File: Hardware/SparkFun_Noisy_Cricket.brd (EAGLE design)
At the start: 31.8 x 25.4 mm, 28 parts, among them U1 LM4853

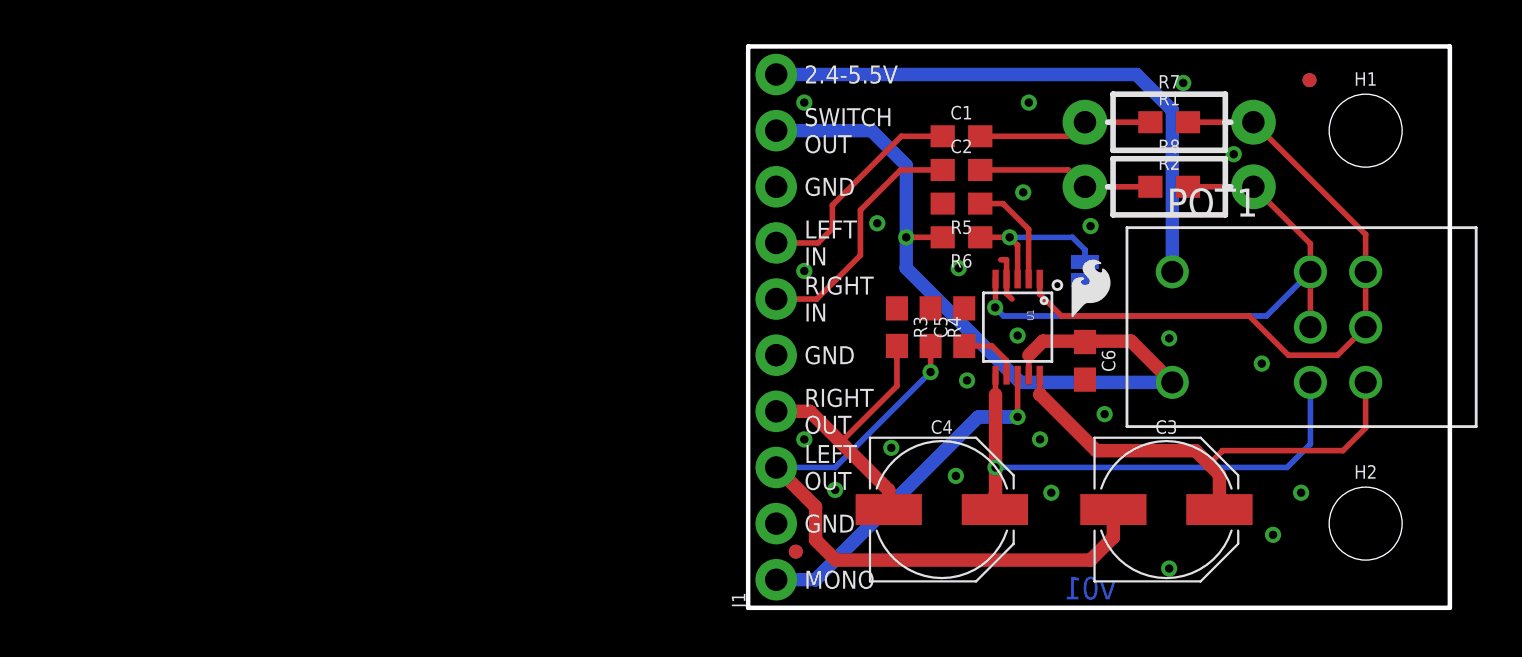
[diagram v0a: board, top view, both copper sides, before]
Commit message: Design Review Changes
- Moved JP1 further away from POT1
- Added JP2 to short C3 and increase bass frequency reponse in mono
operation
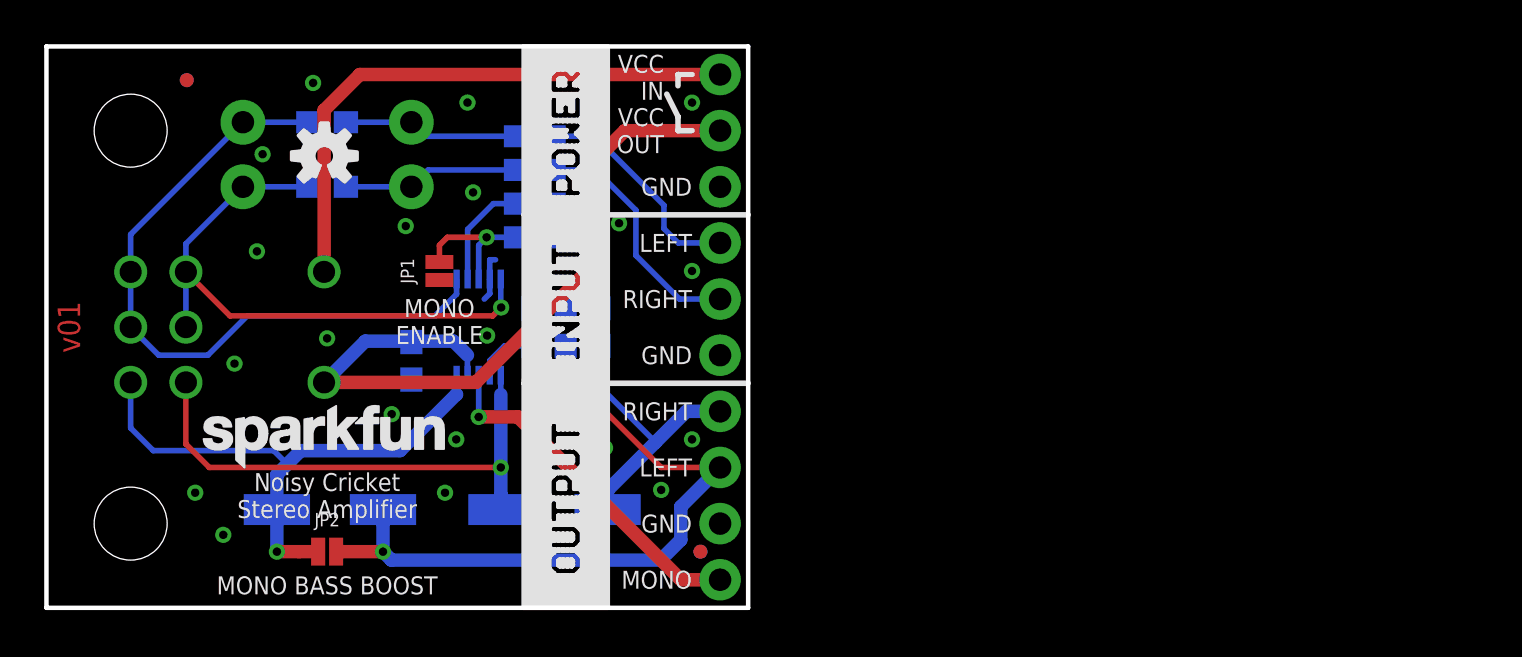
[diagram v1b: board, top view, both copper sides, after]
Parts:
- added JP2: (no value), SparkFun-Jumpers:SMT-JUMPER_2_NO_NO-SILK
- C1, C2: value 0.1uF -> 1.0uF
- moved H1 55.9 mm to (-27.9, 21.6), flipped to the bottom
- moved H2 55.9 mm to (-27.9, 3.81), flipped to the bottom
- moved POT1 55.9 mm to (-27.9, 12.7), flipped to the bottom
- moved FD2 50.8 mm to (-25.4, 23.9), flipped to the bottom
- moved FD4 50.8 mm to (-25.4, 23.9), flipped to the top
- moved LOGO1 50.3 mm to (-25.1, 5.84), flipped to the top
- moved LOGO2 42.5 mm to (-19.2, 20.4), flipped to the top
- moved R1 38.1 mm to (-19.1, 22.0), flipped to the bottom
- moved R2 38.1 mm to (-19.1, 19.1), flipped to the bottom
- moved R7 38.1 mm to (-19.1, 22.0), flipped to the bottom
- moved R8 38.1 mm to (-19.1, 19.1), flipped to the bottom
- moved C3 37.8 mm to (-18.9, 4.45), flipped to the bottom
- moved C6 30.5 mm to (-15.2, 11.2), flipped to the bottom
- moved JP1 29.2 mm to (-14.0, 15.2), flipped to the top
- moved U$1 28.7 mm to (-14.4, 12.8), flipped to the bottom
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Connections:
- removed net N$8: C3.+, POT1.A3, U1.LOUT
- new net LOUT+: C3.+, JP2.1, POT1.A3, U1.LOUT
- net LOUT: now also JP2.2
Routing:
- net LOUT+: track 0.00 -> 25.7 mm, vias 0 -> 1
- net N$8: track 21.9 -> 0.00 mm
- net LOUT: track 29.5 -> 32.0 mm, vias 1 -> 2
- net MODE: track 7.56 -> 6.41 mm
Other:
- board text added: "MONO BASS BOOST"

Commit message: Corrected board position
- Board was saved upside down, corrected by flipping board back around
and resaving.
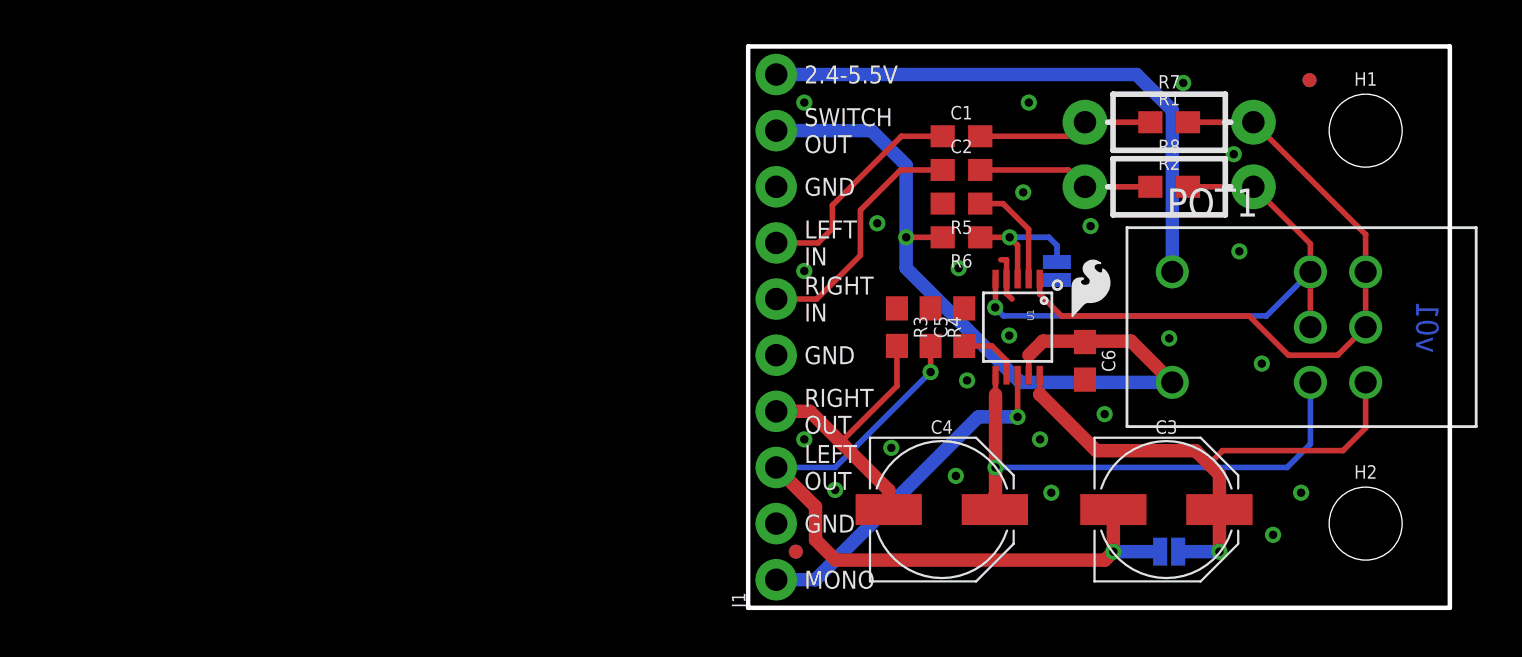
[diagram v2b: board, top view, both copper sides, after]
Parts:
- moved H1 55.9 mm to (27.9, 21.6), flipped to the top
- moved H2 55.9 mm to (27.9, 3.81), flipped to the top
- moved POT1 55.9 mm to (27.9, 12.7), flipped to the top
- moved FD2 50.8 mm to (25.4, 23.9), flipped to the top
- moved FD4 50.8 mm to (25.4, 23.9), flipped to the bottom
- moved LOGO1 50.3 mm to (25.1, 5.84), flipped to the bottom
- moved LOGO2 38.4 mm to (19.2, 20.4), flipped to the bottom
- moved JP2 38.1 mm to (19.1, 2.54), flipped to the bottom
- moved R1 38.1 mm to (19.1, 22.0), flipped to the top
- moved R2 38.1 mm to (19.1, 19.1), flipped to the top
- moved R7 38.1 mm to (19.1, 22.0), flipped to the top
- moved R8 38.1 mm to (19.1, 19.1), flipped to the top
- moved C3 37.8 mm to (18.9, 4.45), flipped to the top
- moved C6 30.5 mm to (15.2, 11.2), flipped to the top
- moved U$1 28.7 mm to (14.4, 12.8), flipped to the top
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
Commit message: v10 Changes
- Replaced C1/C2 with X7R capacitors with a better low end frequency
response.
- Moved C3/C4 further away from POT1.
- Replaced R1/R2 with 2.2k resistors instead of 20k.
- Added lines to top silk to separate Power/Input/Output sections.
- Changed "Mono Enable" silk on bottom layer to "Mono Output".
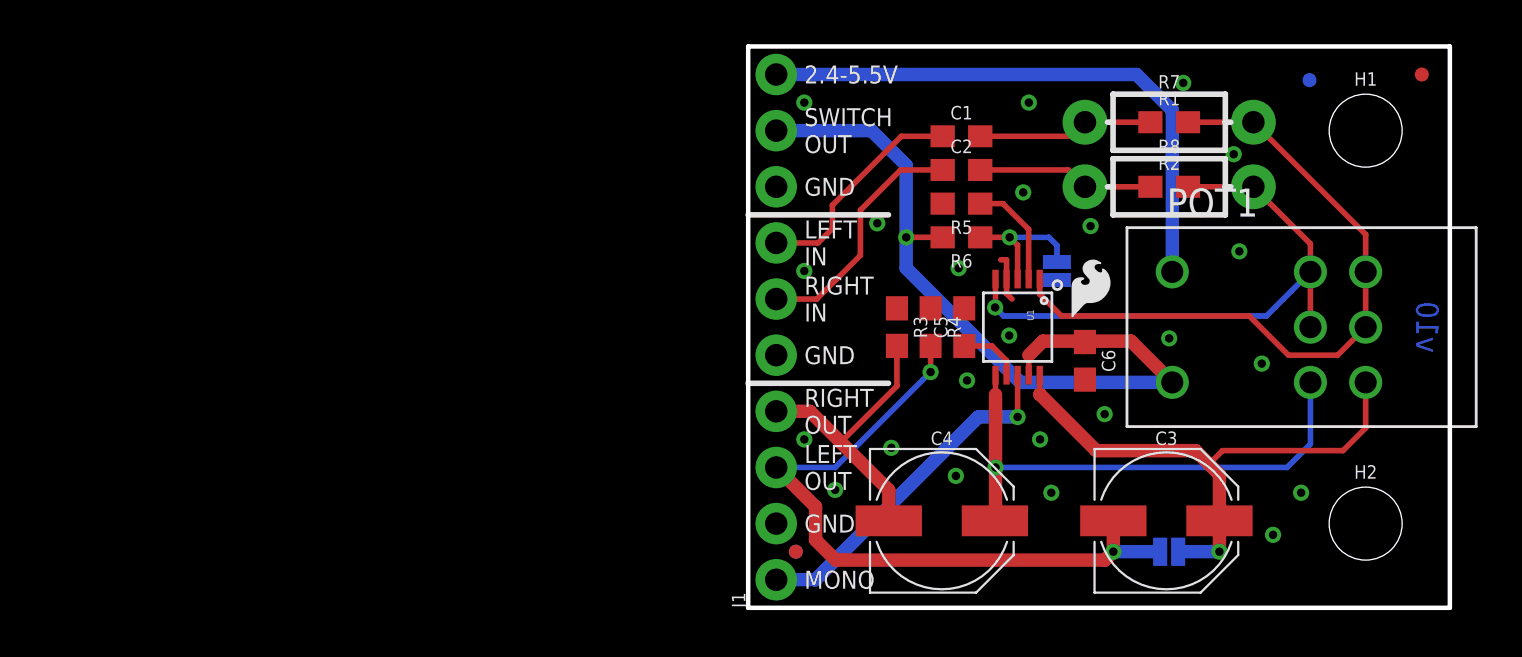
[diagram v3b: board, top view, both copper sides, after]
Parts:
- R1, R2: value 20k -> 2.2k
- moved FD2 5.09 mm to (30.5, 24.1)
- moved POT1 2.54 mm to (25.4, 12.7)
- moved C3 0.51 mm to (18.9, 3.94)
- moved C4 0.51 mm to (8.76, 3.94)
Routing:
- net LOUT: track 32.0 -> 31.5 mm
- net ROUT: track 12.9 -> 13.4 mm
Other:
- board text added: "MONO OUTPUT"
- board text added: "Units: Inches"
- board text added: "v10"
- board text removed: "MONO ENABLE"
- board text removed: "v01"
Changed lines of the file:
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@@
 <layer number="20" name="Dimension" color="15" fill="1" visible="yes" active="yes"/>
 <layer number="21" name="tPlace" color="16" fill="1" visible="yes" active="yes"/>
-<layer number="22" name="bPlace" color="14" fill="1" visible="no" active="yes"/>
+<layer number="22" name="bPlace" color="14" fill="1" visible="yes" active="yes"/>
 <layer number="23" name="tOrigins" color="15" fill="1" visible="yes" active="yes"/>
-<layer number="24" name="bOrigins" color="15" fill="1" visible="no" active="yes"/>
+<layer number="24" name="bOrigins" color="15" fill="1" visible="yes" active="yes"/>
 <layer number="25" name="tNames" color="7" fill="1" visible="no" active="yes"/>
 <layer number="26" name="bNames" color="7" fill="1" visible="no" active="yes"/>
@@
 <layer number="45" name="Holes" color="7" fill="1" visible="no" active="yes"/>
 <layer number="46" name="Milling" color="3" fill="1" visible="no" active="yes"/>
-<layer number="47" name="Measures" color="7" fill="1" visible="no" active="yes"/>
+<layer number="47" name="Measures" color="7" fill="1" visible="yes" active="yes"/>
 <layer number="48" name="Document" color="7" fill="1" visible="no" active="yes"/>
 <layer number="49" name="Reference" color="7" fill="1" visible="no" active="yes"/>
@@
 <layer number="59" name="tCarbon" color="7" fill="1" visible="no" active="no"/>
 <layer number="60" name="bCarbon" color="7" fill="1" visible="no" active="no"/>
+<layer number="88" name="SimResults" color="9" fill="1" visible="yes" active="yes"/>
+<layer number="89" name="SimProbes" color="9" fill="1" visible="yes" active="yes"/>
 <layer number="90" name="Modules" color="5" fill="1" visible="no" active="no"/>
 <layer number="91" name="Nets" color="2" fill="1" visible="no" active="no"/>
@@
 <text x="2.54" y="1.27" size="0.8128" layer="22" font="vector" ratio="15" rot="MR180" align="center-left">MONO</text>
 <text x="13.97" y="12.954" size="0.8128" layer="22" font="vector" ratio="15" rot="MR180" align="center">MONO
-ENABLE</text>
+OUTPUT</text>
 <dimension x1="0" y1="0" x2="0" y2="25.4" x3="-5.08" y3="12.7" textsize="1.27" textratio="15" layer="47" unit="inch"/>
 <dimension x1="0" y1="0" x2="31.75" y2="0" x3="15.875" y3="-5.08" textsize="1.27" textratio="15" layer="47" unit="inch"/>
@@
 <dimension x1="27.94" y1="21.59" x2="31.75" y2="21.59" x3="29.845" y3="33.02" textsize="1.27" textratio="15" layer="47" unit="inch"/>
 <text x="17.78" y="-19.05" size="1.778" layer="51" font="vector" ratio="15">Alex Wende</text>
-<text x="31.242" y="12.7" size="1.016" layer="16" font="vector" ratio="20" rot="MR90" align="top-center">v01</text>
+<text x="31.242" y="12.7" size="1.016" layer="16" font="vector" ratio="20" rot="MR90" align="top-center">v10</text>
 <wire x1="8.5861" y1="23.6489" x2="8.5861" y2="23.8954" width="0.2032" layer="22"/>
 <wire x1="8.5861" y1="23.8954" x2="8.5852" y2="23.8963" width="0.2032" layer="22"/>
@@
 <wire x1="3.175" y1="24.13" x2="3.175" y2="23.622" width="0.254" layer="22"/>
 <text x="19.05" y="1.016" size="0.8128" layer="22" font="vector" ratio="15" rot="MR0" align="center">MONO BASS BOOST</text>
+<wire x1="0" y1="10.16" x2="6.35" y2="10.16" width="0.254" layer="21"/>
+<wire x1="0" y1="17.78" x2="6.35" y2="17.78" width="0.254" layer="21"/>
+<text x="7.62" y="-7.62" size="1.27" layer="47" font="vector" ratio="15">Units: Inches</text>
 </plain>
 <attributes>
@@
 <attribute name="PROD_ID" value="CAP-00868" x="9.652" y="19.812" size="1.778" layer="27" display="off"/>
 </element>
-<element name="C3" library="SparkFun-Capacitors" package="PANASONIC_D" value="100uF" x="18.923" y="4.445">
-<attribute name="PROD_ID" value="CAP-12547" x="18.923" y="4.445" size="1.778" layer="27" display="off"/>
-</element>
-<element name="C4" library="SparkFun-Capacitors" package="PANASONIC_D" value="100uF" x="8.763" y="4.445">
-<attribute name="PROD_ID" value="CAP-12547" x="8.763" y="4.445" size="1.778" layer="27" display="off"/>
+<element name="C3" library="SparkFun-Capacitors" package="PANASONIC_D" value="100uF" x="18.923" y="3.937">
+<attribute name="PROD_ID" value="CAP-12547" x="18.923" y="3.937" size="1.778" layer="27" display="off"/>
+</element>
+<element name="C4" library="SparkFun-Capacitors" package="PANASONIC_D" value="100uF" x="8.763" y="3.937">
+<attribute name="PROD_ID" value="CAP-12547" x="8.763" y="3.937" size="1.778" layer="27" display="off"/>
 </element>
 <element name="C5" library="SparkFun-Capacitors" package="0603" value="1.0uF" x="9.779" y="12.7" rot="R90">
@@
 <element name="FRAME1" library="SparkFun-Aesthetics" package="CREATIVE_COMMONS" value="FRAME-LETTER" x="-13.97" y="-19.05"/>
 <element name="JP1" library="SparkFun-Jumpers" package="SMT-JUMPER_2_NO_NO-SILK" value="" x="13.97" y="15.24" rot="MR90"/>
-<element name="POT1" library="SparkFun-Resistors" package="POT-DUAL-SWITCH-PTH" value="20k" x="27.94" y="12.7">
-<attribute name="PROD_ID" value="RES-13814" x="27.94" y="12.7" size="1.778" layer="27" display="off"/>
-</element>
-<element name="R1" library="SparkFun-Resistors" package="0603" value="20k" x="19.05" y="21.971">
-<attribute name="PROD_ID" value="RES-09383" x="19.05" y="21.971" size="1.778" layer="27" display="off"/>
-</element>
-<element name="R2" library="SparkFun-Resistors" package="0603" value="20k" x="19.05" y="19.05">
-<attribute name="PROD_ID" value="RES-09383" x="19.05" y="19.05" size="1.778" layer="27" display="off"/>
+<element name="POT1" library="SparkFun-Resistors" package="POT-DUAL-SWITCH-PTH" value="20k" x="25.4" y="12.7">
+<attribute name="PROD_ID" value="RES-13814" x="25.4" y="12.7" size="1.778" layer="27" display="off"/>
+<attribute name="VALUE" value="20k" x="25.4" y="12.7" size="1.778" layer="27" display="off"/>
+</element>
+<element name="R1" library="SparkFun-Resistors" package="0603" value="2.2k" x="19.05" y="21.971">
+<attribute name="PROD_ID" value="RES-08272" x="19.05" y="21.971" size="1.778" layer="27" display="off"/>
+</element>
+<element name="R2" library="SparkFun-Resistors" package="0603" value="2.2k" x="19.05" y="19.05">
+<attribute name="PROD_ID" value="RES-08272" x="19.05" y="19.05" size="1.778" layer="27" display="off"/>
 </element>
 <element name="R3" library="SparkFun-Resistors" package="0603" value="1k" x="6.731" y="12.7" rot="R270">
@@
 </element>
 <element name="FD1" library="SparkFun-Aesthetics" package="FIDUCIAL-MICRO" value="FIDUCIALUFIDUCIAL" x="2.159" y="2.54"/>
-<element name="FD2" library="SparkFun-Aesthetics" package="FIDUCIAL-MICRO" value="FIDUCIALUFIDUCIAL" x="25.4" y="23.876"/>
+<element name="FD2" library="SparkFun-Aesthetics" package="FIDUCIAL-MICRO" value="FIDUCIALUFIDUCIAL" x="30.48" y="24.13"/>
 <element name="FD3" library="SparkFun-Aesthetics" package="FIDUCIAL-MICRO" value="FIDUCIALUFIDUCIAL" x="2.159" y="2.54" rot="MR0"/>
 <element name="FD4" library="SparkFun-Aesthetics" package="FIDUCIAL-MICRO" value="FIDUCIALUFIDUCIAL" x="25.4" y="23.876" rot="MR0"/>
@@
 <wire x1="20.241059375" y1="7.112" x2="20.85203125" y2="6.501028125" width="0.6096" layer="1"/>
 <wire x1="20.85203125" y1="6.501028125" x2="21.323" y2="6.030059375" width="0.6096" layer="1"/>
-<wire x1="21.323" y1="6.030059375" x2="21.323" y2="4.445" width="0.6096" layer="1"/>
+<wire x1="21.323" y1="6.030059375" x2="21.323" y2="3.937" width="0.6096" layer="1"/>
 <wire x1="13.192" y1="9.652" x2="13.208" y2="9.652" width="0.6096" layer="1"/>
 <wire x1="13.208" y1="9.652" x2="15.748" y2="7.112" width="0.6096" layer="1"/>
@@
 <wire x1="21.463" y1="7.111996875" x2="20.85203125" y2="6.501028125" width="0.254" layer="1"/>
 <contactref element="JP2" pad="1"/>
-<wire x1="21.323" y1="4.445" x2="21.323" y2="2.54" width="0.6096" layer="1"/>
+<wire x1="21.323" y1="3.937" x2="21.323" y2="2.54" width="0.6096" layer="1"/>
 <via x="21.323" y="2.54" extent="1-16" drill="0.381"/>
 <wire x1="21.323" y1="2.54" x2="19.4564" y2="2.54" width="0.6096" layer="16"/>
@@
 <wire x1="18.6436" y1="2.54" x2="16.523" y2="2.54" width="0.6096" layer="16"/>
 <via x="16.523" y="2.54" extent="1-16" drill="0.381"/>
-<wire x1="16.523" y1="2.54" x2="16.523" y2="4.445" width="0.6096" layer="1"/>
+<wire x1="16.523" y1="2.54" x2="16.523" y2="3.937" width="0.6096" layer="1"/>
 </signal>
 <signal name="ROUT">
@@
 <wire x1="6.731" y1="11.85" x2="6.731" y2="10.033" width="0.254" layer="1"/>
 <wire x1="6.731" y1="10.033" x2="4.1901125" y2="7.4921125" width="0.254" layer="1"/>
-<wire x1="6.363" y1="5.319225" x2="6.363" y2="4.445" width="0.6096" layer="1"/>
+<wire x1="6.363" y1="5.319225" x2="6.363" y2="3.937" width="0.6096" layer="1"/>
 </signal>
 <signal name="N$9">
@@
 <via x="11.192" y="6.35" extent="1-16" drill="0.381"/>
 <wire x1="11.192" y1="9.652" x2="11.192" y2="6.35" width="0.6096" layer="1"/>
-<wire x1="11.192" y1="6.35" x2="11.192" y2="5.08" width="0.6096" layer="1"/>
-<wire x1="11.192" y1="5.08" x2="11.163" y2="5.08" width="0.6096" layer="1"/>
-<wire x1="11.163" y1="5.08" x2="11.163" y2="4.445" width="0.6096" layer="1"/>
+<wire x1="11.192" y1="6.35" x2="11.192" y2="3.966" width="0.6096" layer="1"/>
+<wire x1="11.192" y1="3.966" x2="11.163" y2="3.937" width="0.6096" layer="1"/>
 </signal>
 <signal name="LIN">
